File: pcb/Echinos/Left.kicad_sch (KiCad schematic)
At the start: 30 parts, among them J1 USB_C_Receptacle_USB2.0, J206 Conn_01x06_Pin, J4 FPC_VIK, J5 SATA-7p, J6 Conn_01x07_Pin, J7 Conn_01x07_Pin, U3 SRV05-4, U5 XC6210B332MR-G, U7 SRV05-4

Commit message: ♻️ [PCB] - Remove spreading on the left of the index (outer columns) because it push the upper pinky key farther (it was important to make easier to reach pinky keys on the outer side of the pinky column but I remove it). Improve ground routing and via size when possible.
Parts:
- J5: footprint Echinos:SATA_1x07_P1.27mm_SMD -> Echinos:SATA_1x07_P1.27mm_pads_SMD
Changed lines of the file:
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@@
       (effects (font (size 1.27 1.27)) (justify left))
     )
-    (property "Footprint" "Echinos:SATA_1x07_P1.27mm_SMD" (at 229.87 54.61 0)
+    (property "Footprint" "Echinos:SATA_1x07_P1.27mm_pads_SMD" (at 229.87 54.61 0)
       (effects (font (size 1.27 1.27)) (justify bottom) hide)
     )

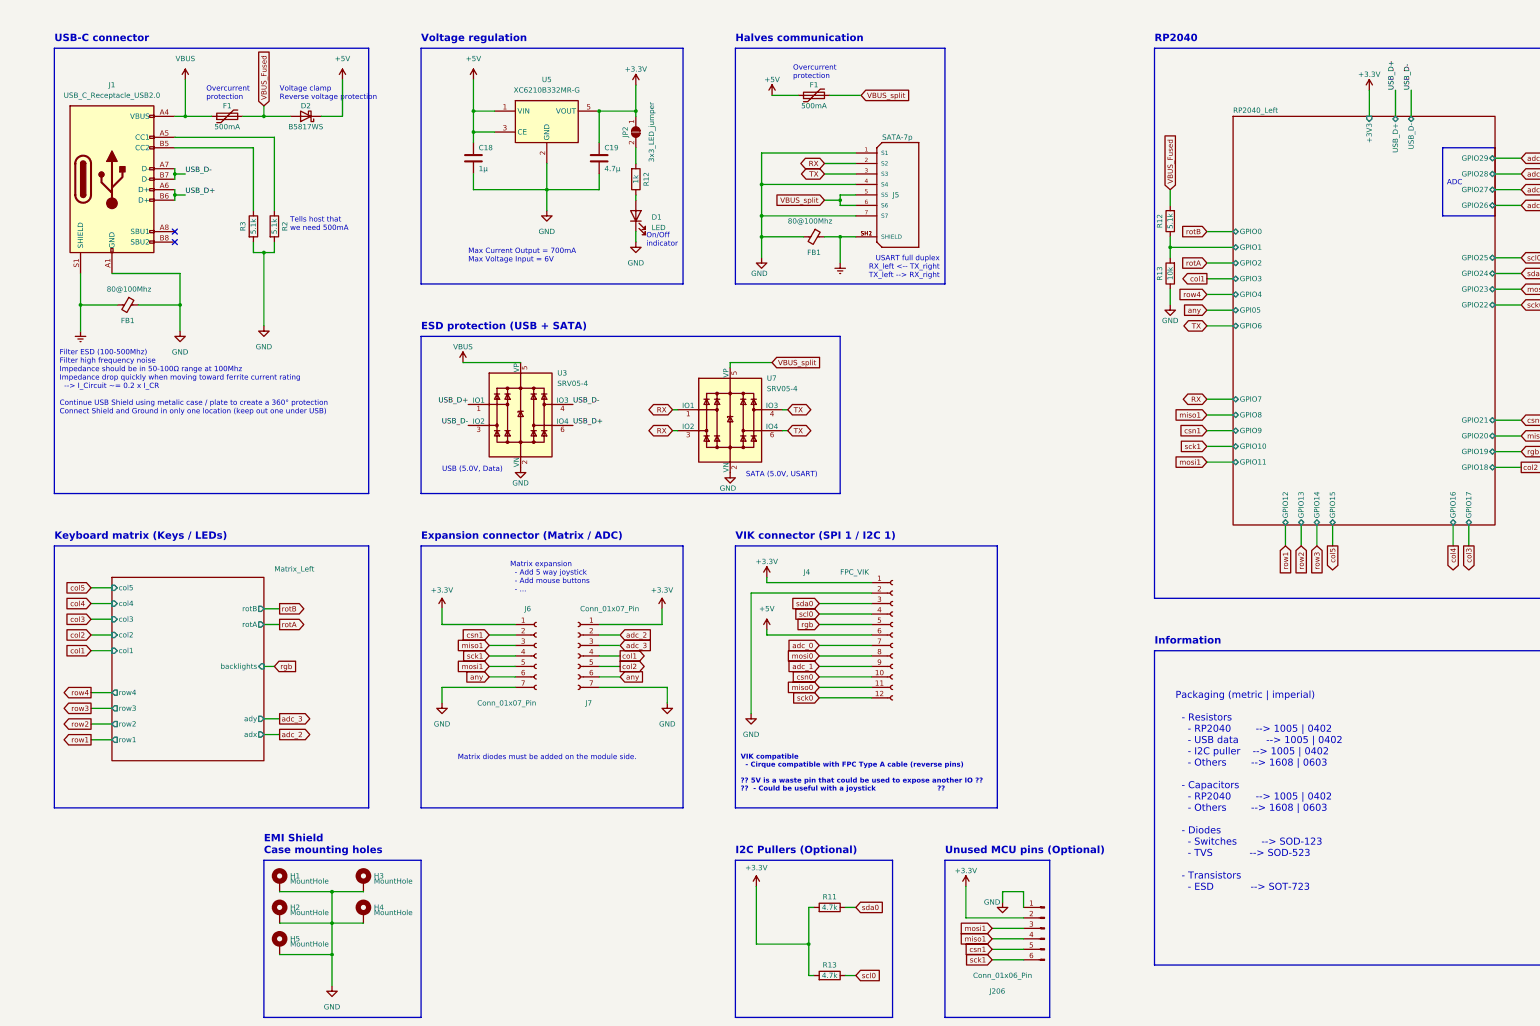
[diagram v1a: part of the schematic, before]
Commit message: [PCB] - Save last state with in-board MCU.
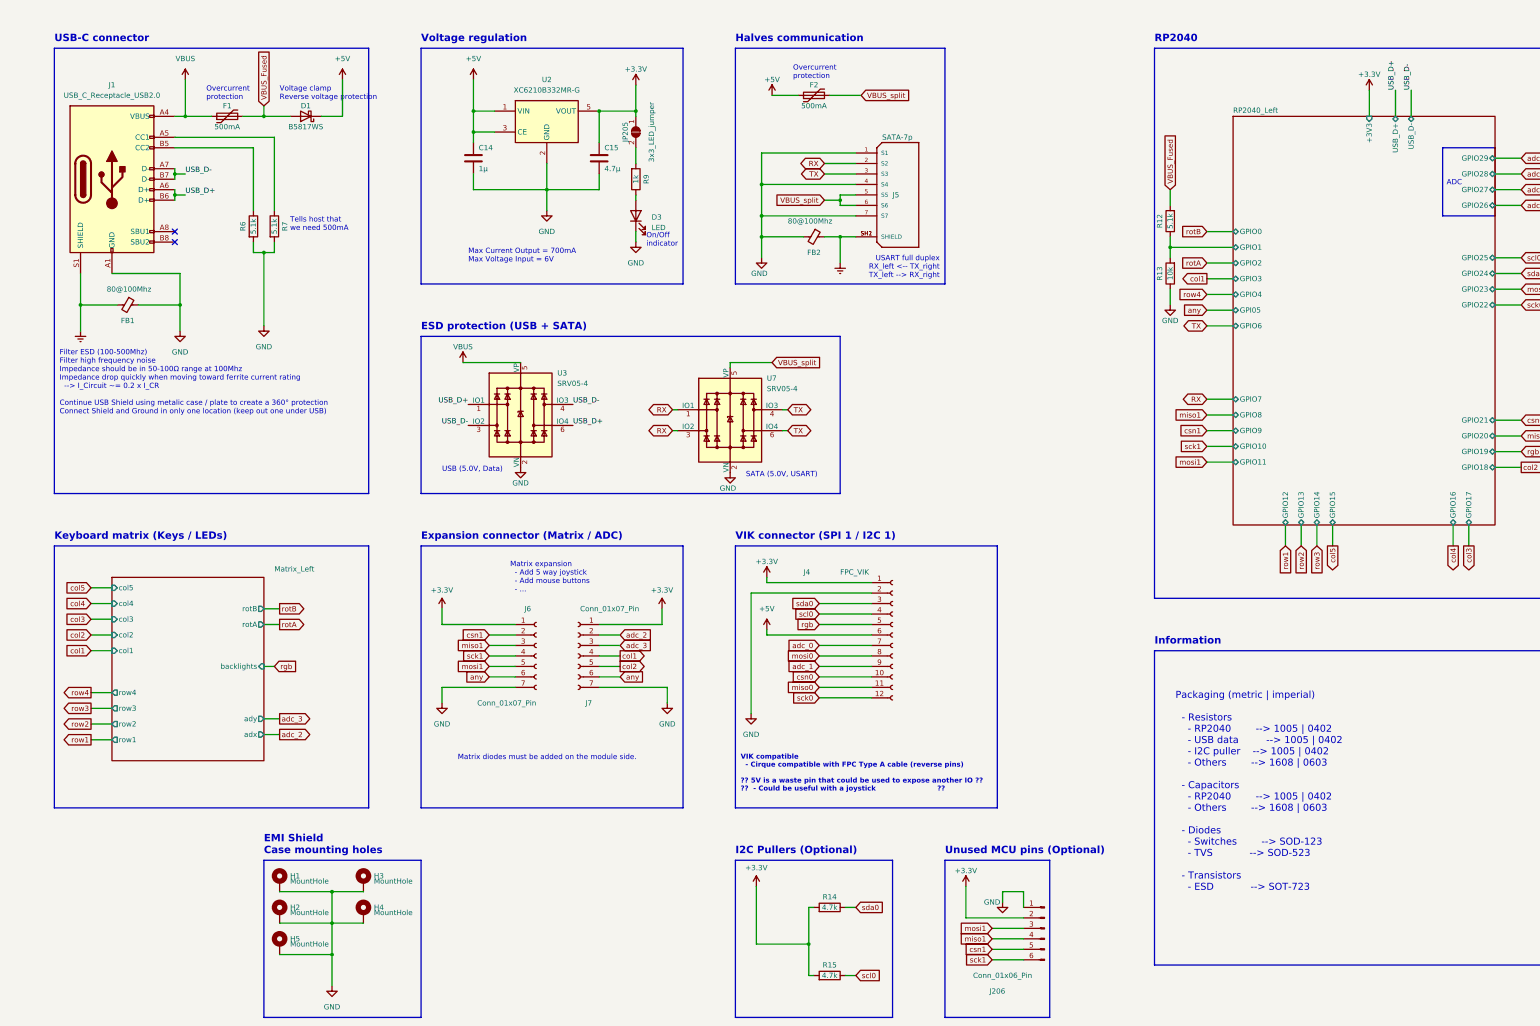
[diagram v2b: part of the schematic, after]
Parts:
- renumbered C18 to C14, C19 to C15, D2 to D1, D1 to D3, F1 to F2, FB1 to FB2, JP2 to JP205, R11 to R14, R13 to R15, R3 to R6, R2 to R7, R12 to R9, U5 to U2

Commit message: [PCB] - Save last state with Gemini MCU board (with mod exposing more pins).
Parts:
- removed C14: 1µ, Capacitor_SMD:C_0603_1608Metric_Pad1.08x0.95mm_HandSolder, symbol Device:C
- removed C15: 4.7µ, Capacitor_SMD:C_0603_1608Metric_Pad1.08x0.95mm_HandSolder, symbol Device:C
- removed D1: B5817WS, Diode_SMD:D_SOD-323_HandSoldering, symbol Device:D_Schottky
- removed D3: LED, Diode_SMD:D_SOD-323_HandSoldering, symbol Device:LED
- removed F1: 500mA, Fuse:Fuse_0603_1608Metric_Pad1.05x0.95mm_HandSolder, symbol Device:Polyfuse
- removed FB1: 80@100Mhz, Inductor_SMD:L_0805_2012Metric_Pad1.15x1.40mm_HandSolder, symbol Device:FerriteBead_Small
- removed J1: USB_C_Receptacle_USB2.0, Connector_USB:USB_C_Receptacle_HRO_TYPE-C-31-M-12, symbol Connector:USB_C_Receptacle_USB2.0
- removed JP205: 3x3_LED_jumper, Echinos:SolderJumper_Open_0.8x1.2mm, symbol Jumper:SolderJumper_2_Open
- removed R12, R6, R7: 5.1k, Resistor_SMD:R_0402_1005Metric_Pad0.72x0.64mm_HandSolder, symbol Device:R
- removed R13: 10k, Resistor_SMD:R_0402_1005Metric_Pad0.72x0.64mm_HandSolder, symbol Device:R
- removed R9: 1k, Resistor_SMD:R_0402_1005Metric_Pad0.72x0.64mm_HandSolder, symbol Device:R
- removed U2: XC6210B332MR-G, Package_TO_SOT_SMD:SOT-23-5_HandSoldering, symbol Regulator_Linear:XC6210B332MR
- removed U3: SRV05-4, Package_TO_SOT_SMD:SOT-23-6, symbol Power_Protection:SRV05-4
- added JP0, JP1: SolderJumper_2_Bridged, Jumper:SolderJumper-2_P1.3mm_Bridged_Pad1.0x1.5mm, symbol Jumper:SolderJumper_2_Bridged
- added JP2, JP3, JP4: Jumper_2_Open, Jumper:SolderJumper-2_P1.3mm_Open_Pad1.0x1.5mm, symbol Jumper:Jumper_2_Open
- added U1: RP2040-zero, Echinos:RP2040-Gemini-Mod, symbol Echinos:RP2040-zero
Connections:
- net +3.3V: now also JP3.1 (A), JP4.1 (A), U1.30 (3V3); no longer R14.2, R15.2
- net +5V: now also JP0.1 (A), U1.32 (VCC); no longer J4.6 (Pin_6)
- net GND: now also U1.31 (GND)
- net RX: now also J5.3 (S3), U7.4 (IO3), U7.6 (IO4), U1.1 (GPIO1); no longer J5.2 (S2), U7.1 (IO1), U7.3 (IO2)
- net TX: now also J5.2 (S2), U7.1 (IO1), U7.3 (IO2), U1.0 (GPIO0); no longer J5.3 (S3), U7.4 (IO3), U7.6 (IO4)
- net adc_0: now also U1.26 (GPIO26_ADC0)
- net adc_1: now also U1.27 (GPIO27_ADC1)
- net col1: now also U1.6 (GPIO6)
- net col2: now also U1.5 (GPIO5)
- net col3: now also U1.4 (GPIO4)
- net col4: now also U1.3 (GPIO3)
- net col5: now also U1.2 (GPIO2)
- net csn0: no longer J4.10 (Pin_10)
- net csn1: now also J4.10 (Pin_10), U1.13 (GPIO13)
- net miso0: no longer J4.11 (Pin_11)
- net miso1: now also J4.11 (Pin_11), U1.12 (GPIO12)
- net mosi0: no longer J4.8 (Pin_8)
- net mosi1: now also J4.8 (Pin_8), U1.15 (GPIO15)
- net rgb: now also JP1.1 (A), U1.16 (GPIO16); no longer J4.5 (Pin_5)
- net row1: now also U1.10 (GPIO10)
- net row2: now also U1.11 (GPIO11)
- net row3: now also U1.9 (GPIO9)
- net row4: now also U1.8 (GPIO8)
- net sck0: no longer J4.12 (Pin_12)
- net sck1: now also J4.12 (Pin_12), U1.14 (GPIO14)
- net scl0: now also U1.28 (GPIO28_ADC2)
- net sda0: now also U1.29 (GPIO29_ADC3)
- new net: JP3.2 (B), R14.2
- new net: JP4.2 (B), R15.2
- new net: J4.6 (Pin_6), JP0.2 (B)
- new net LED_left/backlight_in: JP1.2 (B), JP2.1 (A)
- new net rgb_out: J4.5 (Pin_5), JP2.2 (B)
- new net row5: U1.7 (GPIO7)
- no-connect marks 2 -> 3
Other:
- removed sheet RP2040_Left
- added sheet LED_left (LED_left.kicad_sch)
- sheet Matrix_Left ports: added row5; removed backlights, rotA, rotB
- note added: "Bridge it to disable RGB blacklight on keyboard"
- note added: "Cut it to disable RGB on VIK modules."
- note added: "Halves communication (SERIAL_USART_FULL_DUPLEX)"
- note added: "Keyboard RGB (leds)"
- note added: "Keyboard matrix (Keys)"
- note added: "Responsibility of using pull up resistors is on the VIK modules. PCB pull up resistors are opt-in."
- note added: "TODO --------- [ ] Add rst pin to mcu board pcb"
- note added: "This jumper is not standard and is *not* required. Cut it if one want to connect a cirque trackpad directly via SPI."
- note added: "VIK compatible - Cirque compatible with FPC Type A cable (reverse pins)"
- note added: "VIK connector (SPI 1 / I2C 0)"
- note added: "With STM32 MCUs one can swap Rx and Tx at the software level --> Adding hardware selection is optionnal https://docs.qmk.fm/drivers/serial#setup-2"
- note removed: "Design rules ---------"
- note removed: "ESD protection - VBUS + IO --> ElecSuper USBLC6-2P6-ES (5V, 3 lines, SOT-563) - VBUS --> Texas Instruments TVS0500DRVR (0.39) --> Texas Instruments TPD1E10B06QDPYRQ1 (1.11) - IO --> Born ESD7L5.0DT5G-N (5V, 2 lines, SOT 723) (0.13) --> Texas Instruments TPD2E2U06 (TODO)"
- note removed: "Filter ESD (100-500Mhz) Filter high frequency noise Impedance should be in 50-100Ω range at 100Mhz Impedance drop quickly when moving toward ferrite current rating --> I_Circuit ~= 0.2 x I_CR Continue USB Shield using metalic case / plate to create a 360° protection Connect Shield and Ground in only one location (keep out one under USB)"
- note removed: "Halves communication"
- note removed: "Keyboard matrix (Keys / LEDs)"
- note removed: "Max Current Output = 700mA Max Voltage Input = 6V"
- note removed: "On/Off indicator"
- note removed: "SATA (5.0V, USART)"
- note removed: "Tells host that we need 500mA"
- note removed: "USB (5.0V, Data)"
- note removed: "USB-C connector"
- note removed: "VIK compatible - Cirque compatible with FPC Type A cable (reverse pins) ?? 5V is a waste pin that could be used to expose another IO ?? ?? - Could be useful with a joystick ??"
- note removed: "VIK connector (SPI 1 / I2C 1)"
- note removed: "Voltage clamp Reverse voltage protection"
- note removed: "Voltage regulation"
- moved on the sheet: F2, FB2, H1, H2, H3, H4, H5, J206, J4, J5, J6, J7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

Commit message: [PCB] - Save last state with Helios MCU board and gasket tabs on PCB.
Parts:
- removed FB2: 80@100Mhz, Inductor_SMD:L_0805_2012Metric_Pad1.15x1.40mm_HandSolder, symbol Device:FerriteBead_Small
- removed J206: Conn_01x06_Pin, Connector_PinSocket_2.00mm:PinSocket_1x06_P2.00mm_Horizontal, symbol Connector:Conn_01x06_Pin
- removed J4: FPC_VIK, Connector_FFC-FPC:Hirose_FH12-12S-0.5SH_1x12-1MP_P0.50mm_Horizontal, symbol Connector:Conn_01x12_Socket
- removed J6, J7: Conn_01x07_Pin, Connector_PinHeader_2.54mm:PinHeader_1x07_P2.54mm_Vertical, symbol Connector:Conn_01x07_Socket
- removed U1: RP2040-zero, Echinos:RP2040-Gemini-Mod, symbol Echinos:RP2040-zero
- added H6: MountHole, MountingHole:MountingHole_3.2mm_M3_Pad, symbol Mechanical:MountingHole_Pad
- added J1, J2, J3: Conn_01x06_Socket, Connector_FFC-FPC:Hirose_FH12-6S-0.5SH_1x06-1MP_P0.50mm_Horizontal, symbol Connector:Conn_01x06_Socket
- added J4: ~, Connector_FFC-FPC:Hirose_FH12-12S-0.5SH_1x12-1MP_P0.50mm_Horizontal, symbol Vik:vik-keyboard-connector
- added JP15, JP16: Jumper_2_Open, Jumper:SolderJumper-2_P1.3mm_Open_Pad1.0x1.5mm, symbol Jumper:Jumper_2_Open
- added R15, R16: 4.7k, Resistor_SMD:R_0805_2012Metric_Pad1.20x1.40mm_HandSolder, symbol Device:R
- added SW1: Reset, Button_Switch_SMD:SW_SPST_TL3342, symbol Switch:SW_Push
- added U1: Helios, Echinos:Helios_AH_USBdn, symbol PCM_marbastlib-promicroish:Helios
- F2: footprint Fuse:Fuse_0603_1608Metric_Pad1.05x0.95mm_HandSolder -> Fuse:Fuse_1206_3216Metric; LCSC C69679 -> C66452
- H1, H2, H3, H4, H5: footprint Echinos:MountingHole_3mm_Pad_Via -> MountingHole:MountingHole_3.2mm_M3_Pad
- JP12: renamed from JP2; value Jumper_2_Open -> Jumper_3_Bridged12; footprint Jumper:SolderJumper-2_P1.3mm_Open_Pad1.0x1.5mm -> Jumper:SolderJumper-3_P1.3mm_Bridged12_Pad1.0x1.5mm_NumberLabels; symbol Jumper:Jumper_2_Open -> Jumper:SolderJumper_3_Bridged12; now left out of the parts list
- R13: renamed from R14; LCSC (none) -> C60816; now not fitted
- R14: renamed from R15; LCSC (none) -> C60816; now not fitted
- renumbered JP1 to JP11, JP3 to JP13, JP4 to JP14
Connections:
- net +3.3V: now also J2.1 (Pin_1), J3.1 (Pin_1), J4.1 (3V3), JP15.1 (A), JP16.1 (A), U1.16 (3V3)
- net +5V: now also J3.2 (Pin_2), U1.13 (5V)
- net Earth: no longer J5.SH1 (SHIELD), J5.SH2 (SHIELD)
- net GND: now also J5.SH1 (SHIELD), J5.SH2 (SHIELD), H6.1, J2.2 (Pin_2), J3.3 (Pin_3), J4.2 (GND), SW1.1, U1.14 (GND), U1.3 (GND), U1.4 (GND)
- net LED_left/backlight_in: no longer JP11.2 (B)
- net RX: now also U1.2 (P1)
- net TX: now also U1.1 (P0)
- net adc_0: now also J2.3 (Pin_3), J4.7 (GP_AD1), U1.20 (P26)
- net adc_1: now also J2.4 (Pin_4), J4.9 (GP_AD2), U1.19 (P27)
- net col1: now also J1.2 (Pin_2), U1.29 (P16)
- net col2: now also J1.3 (Pin_3), J2.6 (Pin_6), U1.8 (P5)
- net col3: now also J1.4 (Pin_4), U1.7 (P4)
- net col4: now also J1.5 (Pin_5), U1.6 (P3)
- net col5: now also J1.6 (Pin_6), U1.5 (P2)
- net csn1: now also J4.10 (SPI_CS), U1.24 (P21)
- net miso1: now also J4.11 (MISO), U1.22 (P20)
- net mosi1: now also J4.8 (MOSI), U1.23 (P23)
- net rgb: now also U1.34 (P25)
- net rgb_out: now also JP12.3 (B), J4.5 (RGB_DO); no longer JP12.2 (B)
- net row1: now also U1.12 (P9)
- net row2: now also U1.25 (P12)
- net row3: now also U1.11 (P8)
- net row4: now also U1.10 (P7)
- net row5: now also U1.9 (P6)
- net row6: now also J1.1 (Pin_1), U1.26 (P13)
- net sck1: now also J4.12 (SCLK), U1.21 (P22)
- net at JP0.2 (B): now also J4.6 (5V)
- net scl0 renamed scl1
- net scl1: now also J4.4 (SCL), U1.27 (P14)
- net sda0 renamed sda1
- net sda1: now also J4.3 (SDA), U1.28 (P15)
- new net: JP15.2 (B), R15.2
- new net: JP16.2 (B), R16.2
- new net: JP11.2 (B), JP12.2 (C)
- new net ps2_clk: J3.5 (Pin_5), R16.1, U1.18 (P28)
- new net ps2_data: J3.4 (Pin_4), R15.1, U1.17 (P29)
- new net ps2_reset: J3.6 (Pin_6), U1.31 (P10)
- new net reset: SW1.2, U1.15 (RST)
- new net row7: J2.5 (Pin_5), U1.30 (P11)
- no-connect marks 3 -> 2
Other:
- note added: ""adc_0" and "adc_1" lines are shared with VIK."
- note added: ""data" and "clk" are 3.3V logic."
- note added: "(optional) Can use RP2040 internal pull-ups"
- note added: "(optional) Level-shift logic is on modules."
- note added: "(optional) Pull-up should be on VIK modules."
- note added: "(optional) Reset logic is on modules."
- note added: "Bridge 23 to bipass the keyboard rgb"
- note added: "Cut it to disable RGB"
- note added: "Diodes are on modules (ColumnToRow to avoid custom scanning)."
- note added: "Expansion connectors"
- note added: "Helios specific - GPIO 25 is level shifted to 5V logic level (RGB) - GPIO 19 is VBUS detection - GPIO 18 is not connected / used - GPIO 24 is not connected / used - GPIO 17 is micro LED (user controlled) - Power LED (Red) disabled by default (can be bridged)"
- note added: "Joysticks / ADC devices - KSilver-JP19 - Joycon - ..."
- note added: "Joysticks like JP19 can be mapped directly to keyboard matrix. (optional) Diodes are on modules."
- note added: "Matrix expansion - 5-way Navigation switch - Mouse buttons - ..."
- note added: "On board MCU reset"
- note added: "Trackpoints and PS/2 devices"
- note added: "VIK compatible (https://github.com/sadekbaroudi/vik) - Cirque compatible with FPC Type A cable (reverse pins)"
- note removed: "Bridge it to disable RGB blacklight on keyboard"
- note removed: "Cut it to disable RGB on VIK modules."
- note removed: "Expansion connector (Matrix / ADC)"
- note removed: "I2C Pullers (Optional)"
- note removed: "Matrix diodes must be added on the module side."
- note removed: "Matrix expansion - Add 5 way joystick - Add mouse buttons - ..."
- note removed: "Responsibility of using pull up resistors is on the VIK modules. PCB pull up resistors are opt-in."
- note removed: "TODO --------- [ ] Add rst pin to mcu board pcb"
- note removed: "Unused MCU pins (Optional)"
- note removed: "VIK compatible - Cirque compatible with FPC Type A cable (reverse pins)"
- moved on the sheet: JP0, JP11, JP13, JP14
